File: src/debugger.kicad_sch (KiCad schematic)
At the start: 29 parts, among them J2 USB_C_Receptacle_USB2.0_14P, U7 RP2040, U8 W25Q128JVS, U9 NCP1117-1.5_SOT223, Y1 ABM8-272-T3

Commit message: revisão da RP2040
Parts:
- added J1: SM03B-SRSS-TB, Connector_JST:JST_SH_SM03B-SRSS-TB_1x03-1MP_P1.00mm_Horizontal, symbol Connector_Generic_MountingPin:Conn_01x03_MountingPin
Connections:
- net GND: now also J1.2 (Pin_2), J1.MP (MountPin)
- net QSPI_SCLK: no longer U7.52 (QSPI_SCLK)
- net QSPI_SD0: no longer U7.53 (QSPI_SD0)
- net QSPI_SD1: no longer U7.55 (QSPI_SD1)
- net QSPI_SD2: no longer U7.54 (QSPI_SD2)
- net QSPI_SD3: no longer U7.51 (QSPI_SD3)
- net QSPI_SS: no longer U7.56 (QSPI_SS)
- net XIN: no longer U7.20 (XIN)
- net XOUT: no longer U7.21 (XOUT)
- net SWCL renamed SWCLK
- net SWCLK: now also J1.1 (Pin_1)
- net UART1 RX renamed UART0 RX
- net UART1 TX renamed UART0 TX
- new net SWD: J1.3 (Pin_3)
- no-connect marks 26 -> 37
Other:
- note added: "CONECTOR"

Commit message: FEAT: adicionando footprints
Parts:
- J2: footprint (none) -> Connector_USB:USB_C_Receptacle_GCT_USB4105-xx-A_16P_TopMnt_Horizontal
- U7: footprint (none) -> componentes_personalizados:RP2040
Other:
- note added: "RP2040"
- moved on the sheet: C17, C18, C43, C44, C45, C47, C48, C49, C50, C51, C52, C59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

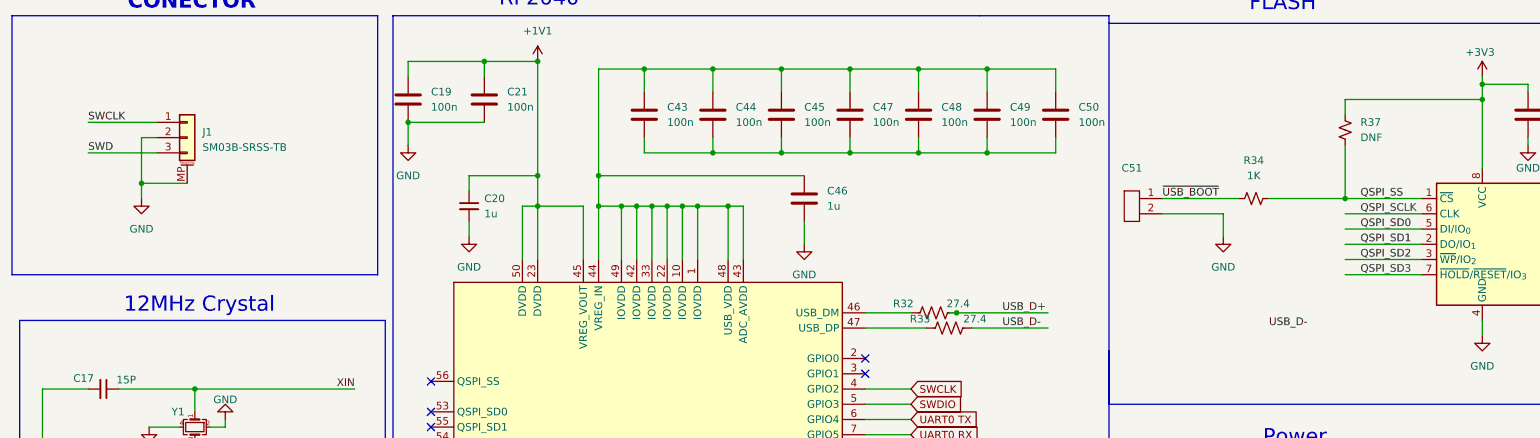
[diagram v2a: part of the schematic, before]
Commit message: adicionado footprints, falta microfone e display somente
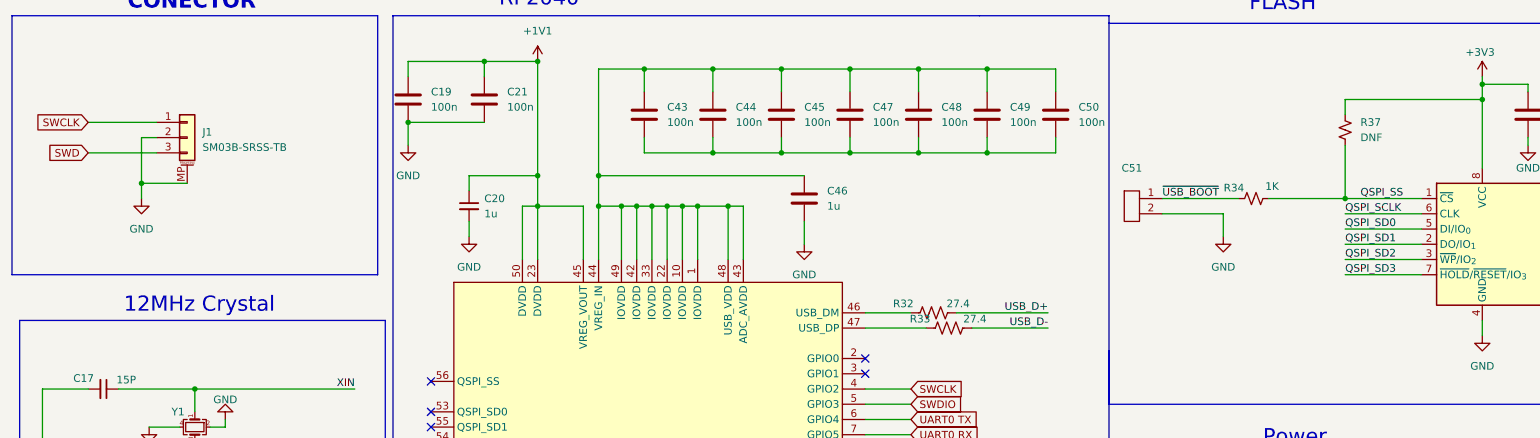
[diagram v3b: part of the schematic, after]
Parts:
- C51: footprint (none) -> Connector_PinHeader_1.00mm:PinHeader_1x02_P1.00mm_Horizontal
- R32, R33: footprint CR0402-FX-27R4GLF -> Resistor_SMD:R_0402_1005Metric
- R34, R37: footprint (none) -> Resistor_SMD:R_0402_1005Metric
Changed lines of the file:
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@@
 	)
 	(junction
-		(at 171.45 68.58)
-		(diameter 0)
-		(color 0 0 0 0)
-	)
-	(junction
 		(at 101.6 50.8)
 		(diameter 0)
@@
 	)
 	(no_connect
+		(at 156.21 76.2)
+	)
+	(no_connect
 		(at 156.21 137.16)
 	)
@@
 	)
 	(no_connect
-		(at 156.21 76.2)
-	)
-	(no_connect
 		(at 156.21 134.62)
 	)
@@
 	)
 	(no_connect
+		(at 156.21 114.3)
+	)
+	(no_connect
 		(at 156.21 78.74)
 	)
@@
 	)
 	(no_connect
-		(at 156.21 114.3)
-	)
-	(no_connect
 		(at 156.21 91.44)
 	)
@@
 	(wire
 		(pts
-			(xy 171.45 68.58) (xy 186.69 68.58)
-		)
-		(stroke
-			(width 0)
-			(type default)
-		)
-	)
-	(wire
-		(pts
 			(xy 133.35 50.8) (xy 135.89 50.8)
 		)
@@
 	(wire
 		(pts
-			(xy 236.22 62.23) (xy 248.92 62.23)
-		)
-		(stroke
-			(width 0)
-			(type default)
-		)
-	)
-	(wire
-		(pts
 			(xy 223.52 118.11) (xy 223.52 116.84)
 		)
@@
 	(wire
 		(pts
-			(xy 236.22 54.61) (xy 248.92 54.61)
-		)
-		(stroke
-			(width 0)
-			(type default)
-		)
-	)
-	(wire
-		(pts
 			(xy 259.08 30.48) (xy 266.7 30.48)
 		)
@@
 	(wire
 		(pts
-			(xy 236.22 59.69) (xy 248.92 59.69)
-		)
-		(stroke
-			(width 0)
-			(type default)
-		)
-	)
-	(wire
-		(pts
 			(xy 101.6 45.72) (xy 101.6 50.8)
 		)
@@
 	(wire
 		(pts
-			(xy 170.18 68.58) (xy 171.45 68.58)
-		)
-		(stroke
-			(width 0)
-			(type default)
-		)
-	)
-	(wire
-		(pts
 			(xy 212.09 125.73) (xy 228.6 125.73)
 		)
@@
 	(wire
 		(pts
+			(xy 236.22 62.23) (xy 248.92 62.23)
+		)
+		(stroke
+			(width 0)
+			(type default)
+		)
+	)
+	(wire
+		(pts
 			(xy 120.65 50.8) (xy 123.19 50.8)
 		)
@@
 		)
 	)
+	(wire
+		(pts
+			(xy 171.45 68.58) (xy 186.69 68.58)
+		)
+		(stroke
+			(width 0)
+			(type default)
+		)
+	)
 	(polyline
 		(pts
@@
 		)
 	)
+	(wire
+		(pts
+			(xy 236.22 59.69) (xy 248.92 59.69)
+		)
+		(stroke
+			(width 0)
+			(type default)
+		)
+	)
 	(polyline
 		(pts
@@
 	(wire
 		(pts
+			(xy 236.22 54.61) (xy 248.92 54.61)
+		)
+		(stroke
+			(width 0)
+			(type default)
+		)
+	)
+	(wire
+		(pts
 			(xy 101.6 50.8) (xy 99.06 50.8)
 		)
@@
 	)
 	(label "QSPI_SD3"
-		(at 238.76 62.23 0)
+		(at 236.22 62.23 0)
 		(effects
 			(font
@@
 		)
 	)
-	(label "USB_D-"
-		(at 223.52 71.12 0)
-		(effects
-			(font
-				(size 1.27 1.27)
-			)
-			(justify left bottom)
-		)
-	)
 	(label "XIN"
 		(at 71.12 81.28 180)
@@
 	)
 	(label "QSPI_SD1"
-		(at 238.76 57.15 0)
+		(at 236.22 57.15 0)
 		(effects
 			(font
@@
 	)
 	(label "QSPI_SD2"
-		(at 238.76 59.69 0)
+		(at 236.22 59.69 0)
 		(effects
 			(font
@@
 	)
 	(label "QSPI_SCLK"
-		(at 238.76 52.07 0)
+		(at 236.22 52.07 0)
 		(effects
 			(font
@@
 	)
 	(label "QSPI_SD0"
-		(at 238.76 54.61 0)
-		(effects
-			(font
-				(size 1.27 1.27)
-			)
-			(justify left bottom)
-		)
-	)
-	(label "SWD"
-		(at 26.67 41.91 0)
+		(at 236.22 54.61 0)
 		(effects
 			(font
@@
 	)
 	(label "USB_D-"
-		(at 179.07 71.12 0)
+		(at 186.69 71.12 180)
 		(effects
 			(font
 				(size 1.27 1.27)
 			)
-			(justify left bottom)
+			(justify right bottom)
 		)
 	)
 	(label "USB_D+"
-		(at 179.07 68.58 0)
+		(at 186.69 68.58 180)
 		(effects
 			(font
 				(size 1.27 1.27)
 			)
-			(justify left bottom)
-		)
-	)
-	(label "SWCLK"
-		(at 26.67 36.83 0)
-		(effects
-			(font
-				(size 1.27 1.27)
-			)
-			(justify left bottom)
+			(justify right bottom)
 		)
 	)
@@
 	(global_label "SWCLK"
 		(shape input)
+		(at 26.67 36.83 180)
+		(fields_autoplaced yes)
+		(effects
+			(font
+				(size 1.27 1.27)
+			)
+			(justify right)
+		)
+		(property "Intersheetrefs" "${INTERSHEET_REFS}"
+			(at 17.4558 36.83 0)
+			(effects
+				(font
+					(size 1.27 1.27)
+				)
+				(justify right)
+				(hide yes)
+			)
+		)
+	)
+	(global_label "SWCLK"
+		(shape input)
 		(at 163.83 81.28 0)
 		(fields_autoplaced yes)
@@
 		)
 	)
+	(global_label "SWD"
+		(shape input)
+		(at 26.67 41.91 180)
+		(fields_autoplaced yes)
+		(effects
+			(font
+				(size 1.27 1.27)
+			)
+			(justify right)
+		)
+		(property "Intersheetrefs" "${INTERSHEET_REFS}"
+			(at 19.7539 41.91 0)
+			(effects
+				(font
+					(size 1.27 1.27)
+				)
+				(justify right)
+				(hide yes)
+			)
+		)
+	)
 	(global_label "SWDIO"
 		(shape input)
@@
 			)
 		)
-		(property "Footprint" ""
+		(property "Footprint" "Connector_PinHeader_1.00mm:PinHeader_1x02_P1.00mm_Horizontal"
 			(at 198.12 45.72 0)
 			(effects
@@
 			)
 		)
-		(property "Footprint" "CR0402-FX-27R4GLF"
+		(property "Footprint" "Resistor_SMD:R_0402_1005Metric"
 			(at 170.434 70.104 90)
 			(effects
@@
 			)
 		)
-		(property "Footprint" ""
+		(property "Footprint" "Resistor_SMD:R_0402_1005Metric"
 			(at 236.22 38.1 0)
 			(effects
@@
 			)
 		)
-		(property "Footprint" "CR0402-FX-27R4GLF"
+		(property "Footprint" "Resistor_SMD:R_0402_1005Metric"
 			(at 167.894 67.564 90)
 			(effects
@@
 		(dnp no)
 		(property "Reference" "R34"
-			(at 220.98 43.18 90)
+			(at 217.678 47.752 90)
 			(effects
 				(font
@@
 		)
 		(property "Value" "1K"
-			(at 220.98 45.72 90)
+			(at 224.028 47.498 90)
 			(effects
 				(font
@@
 			)
 		)
-		(property "Footprint" ""
+		(property "Footprint" "Resistor_SMD:R_0402_1005Metric"
 			(at 220.98 49.53 0)
 			(effects

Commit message: pequenos ajustes nas tags
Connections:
- net SWD is gone; now on net SWDIO: J1.3 (Pin_3)
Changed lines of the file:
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@@
 		)
 	)
-	(global_label "SWD"
+	(global_label "SWDIO"
 		(shape input)
 		(at 26.67 41.91 180)
@@
 		)
 		(property "Intersheetrefs" "${INTERSHEET_REFS}"
-			(at 19.7539 41.91 0)
+			(at 17.8186 41.91 0)
 			(effects
 				(font

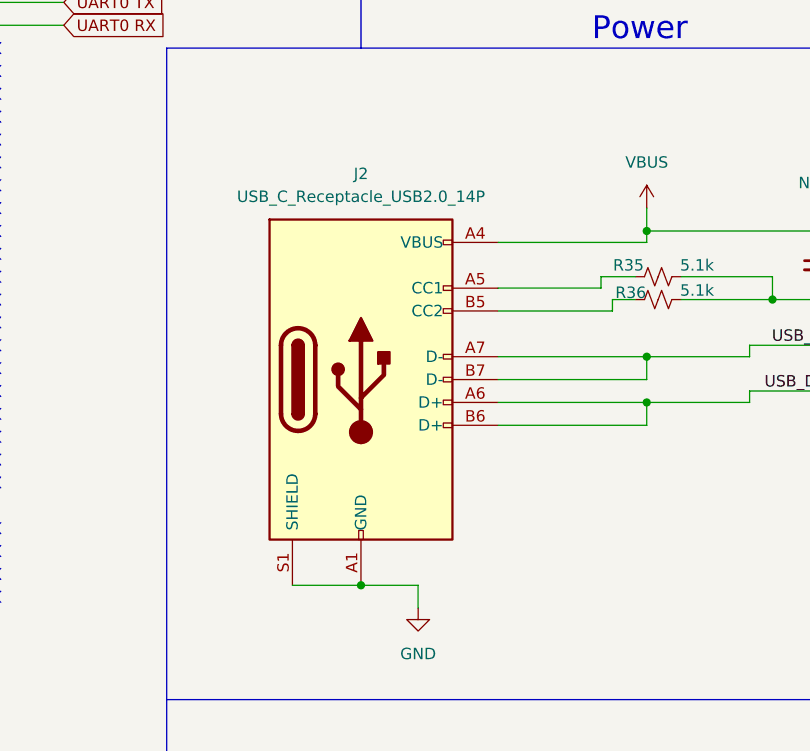
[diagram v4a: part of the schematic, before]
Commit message: Bugs na att da PCI resolvidos (falta só a tela OLED)
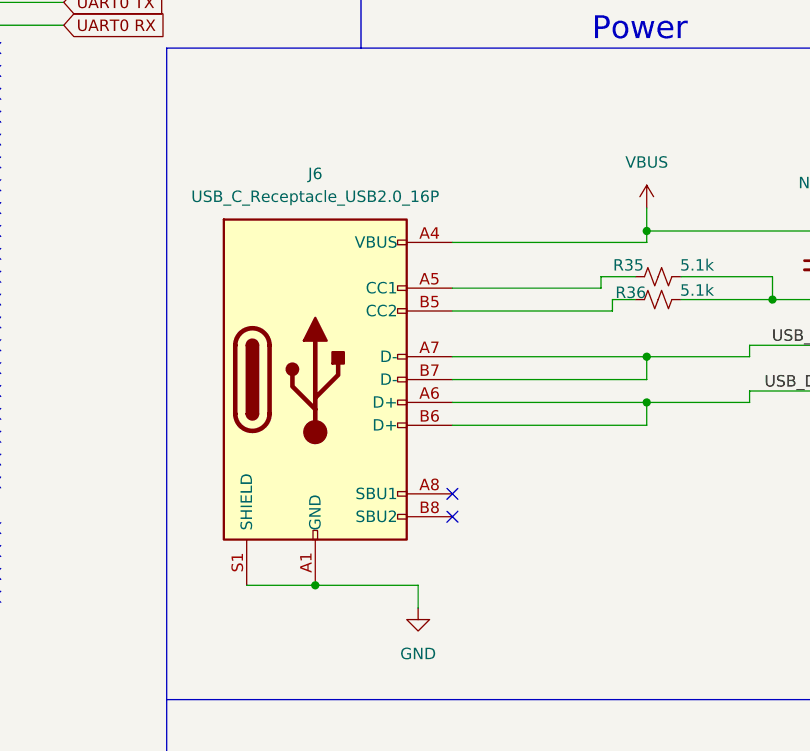
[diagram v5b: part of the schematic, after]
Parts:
- removed J2: USB_C_Receptacle_USB2.0_14P, Connector_USB:USB_C_Receptacle_GCT_USB4105-xx-A_16P_TopMnt_Horizontal, symbol Connector:USB_C_Receptacle_USB2.0_14P
- added J6: USB_C_Receptacle_USB2.0_16P, Connector_USB:USB_C_Receptacle_GCT_USB4105-xx-A_16P_TopMnt_Horizontal, symbol Connector:USB_C_Receptacle_USB2.0_16P
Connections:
- net GND: now also J6.A1 (GND), J6.A12 (GND), J6.B1 (GND), J6.B12 (GND), J6.S1 (SHIELD)
- net USB_D+: now also J6.A6 (D+), J6.B6 (D+)
- net USB_D-: now also J6.A7 (D-), J6.B7 (D-)
- net VBUS: now also J6.A4 (VBUS), J6.A9 (VBUS), J6.B4 (VBUS), J6.B9 (VBUS)
- net at R36.2: now also J6.B5 (CC2)
- net at R35.2: now also J6.A5 (CC1)
- no-connect marks 37 -> 39
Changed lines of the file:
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@@
 	)
 	(junction
+		(at 191.77 151.13)
+		(diameter 0)
+		(color 0 0 0 0)
+	)
+	(junction
 		(at 142.24 27.94)
 		(diameter 0)
@@
 	)
 	(junction
-		(at 196.85 151.13)
-		(diameter 0)
-		(color 0 0 0 0)
-	)
-	(junction
 		(at 101.6 45.72)
 		(diameter 0)
@@
 	)
 	(no_connect
+		(at 207.01 140.97)
+	)
+	(no_connect
 		(at 156.21 111.76)
 	)
@@
 	)
 	(no_connect
+		(at 207.01 143.51)
+	)
+	(no_connect
 		(at 156.21 147.32)
 	)
@@
 	(wire
 		(pts
-			(xy 196.85 151.13) (xy 203.2 151.13)
-		)
-		(stroke
-			(width 0)
-			(type default)
-		)
-	)
-	(wire
-		(pts
 			(xy 26.67 36.83) (xy 38.1 36.83)
 		)
@@
 	(wire
 		(pts
-			(xy 212.09 118.11) (xy 223.52 118.11)
+			(xy 207.01 118.11) (xy 223.52 118.11)
 		)
 		(stroke
@@
 	(wire
 		(pts
+			(xy 191.77 151.13) (xy 203.2 151.13)
+		)
+		(stroke
+			(width 0)
+			(type default)
+		)
+	)
+	(wire
+		(pts
 			(xy 228.6 113.03) (xy 228.6 111.76)
 		)
@@
 	(wire
 		(pts
-			(xy 212.09 125.73) (xy 228.6 125.73)
+			(xy 207.01 125.73) (xy 228.6 125.73)
 		)
 		(stroke
@@
 	(wire
 		(pts
-			(xy 212.09 120.65) (xy 224.79 120.65)
+			(xy 207.01 120.65) (xy 224.79 120.65)
 		)
 		(stroke
@@
 	(wire
 		(pts
-			(xy 212.09 113.03) (xy 228.6 113.03)
+			(xy 207.01 113.03) (xy 228.6 113.03)
 		)
 		(stroke
@@
 	(wire
 		(pts
-			(xy 212.09 130.81) (xy 228.6 130.81)
+			(xy 207.01 130.81) (xy 228.6 130.81)
 		)
 		(stroke
@@
 	(wire
 		(pts
-			(xy 189.23 151.13) (xy 196.85 151.13)
+			(xy 184.15 151.13) (xy 191.77 151.13)
 		)
 		(stroke
@@
 	(wire
 		(pts
-			(xy 228.6 128.27) (xy 212.09 128.27)
+			(xy 228.6 128.27) (xy 207.01 128.27)
 		)
 		(stroke
@@
 	(wire
 		(pts
-			(xy 228.6 133.35) (xy 212.09 133.35)
+			(xy 228.6 133.35) (xy 207.01 133.35)
 		)
 		(stroke
@@
 	)
 	(symbol
-		(lib_id "Connector:USB_C_Receptacle_USB2.0_14P")
-		(at 196.85 128.27 0)
-		(unit 1)
-		(exclude_from_sim no)
-		(in_bom yes)
-		(on_board yes)
-		(dnp no)
-		(fields_autoplaced yes)
-		(property "Reference" "J2"
-			(at 196.85 105.41 0)
-			(effects
-				(font
-					(size 1.27 1.27)
-				)
-			)
-		)
-		(property "Value" "USB_C_Receptacle_USB2.0_14P"
-			(at 196.85 107.95 0)
-			(effects
-				(font
-					(size 1.27 1.27)
-				)
-			)
-		)
-		(property "Footprint" "Connector_USB:USB_C_Receptacle_GCT_USB4105-xx-A_16P_TopMnt_Horizontal"
-			(at 200.66 128.27 0)
-			(effects
-				(font
-					(size 1.27 1.27)
-				)
-				(hide yes)
-			)
-		)
-		(property "Datasheet" "https://www.usb.org/sites/default/files/documents/usb_type-c.zip"
-			(at 200.66 128.27 0)
-			(effects
-				(font
-					(size 1.27 1.27)
-				)
-				(hide yes)
-			)
-		)
-		(property "Description" "USB 2.0-only 14P Type-C Receptacle connector"
-			(at 196.85 128.27 0)
-			(effects
-				(font
-					(size 1.27 1.27)
-				)
-				(hide yes)
-			)
-		)
-		(pin "A6"
-		)
-		(pin "S1"
-		)
-		(pin "A12"
-		)
-		(pin "A4"
-		)
-		(pin "A5"
-		)
-		(pin "B1"
-		)
-		(pin "B5"
-		)
-		(pin "A1"
-		)
-		(pin "B4"
-		)
-		(pin "A7"
-		)
-		(pin "B12"
-		)
-		(pin "B9"
-		)
-		(pin "A9"
-		)
-		(pin "B7"
-		)
-		(pin "B6"
-		)
-		(instances
-			(project "Circuitos Impressos"
-				(path "/49caf936-61f8-45e5-bebd-98db7502d055/3523909c-5026-4ff2-9976-775b6fedfefc"
-					(reference "J2")
-					(unit 1)
-				)
-			)
-		)
-	)
-	(symbol
 		(lib_id "power:GND")
 		(at 36.83 87.63 0)
@@
 					(unit 1)
 				)
+			)
+		)
+	)
+	(symbol
+		(lib_id "Connector:USB_C_Receptacle_USB2.0_16P")
+		(at 191.77 128.27 0)
+		(unit 1)
+		(exclude_from_sim no)
+		(in_bom yes)
+		(on_board yes)
+		(dnp no)
+		(fields_autoplaced yes)
+		(property "Reference" "J6"
+			(at 191.77 105.41 0)
+			(effects
+				(font
+					(size 1.27 1.27)
+				)
+			)
+		)
+		(property "Value" "USB_C_Receptacle_USB2.0_16P"
+			(at 191.77 107.95 0)
+			(effects
+				(font
+					(size 1.27 1.27)
+				)
+			)
+		)
+		(property "Footprint" "Connector_USB:USB_C_Receptacle_GCT_USB4105-xx-A_16P_TopMnt_Horizontal"
+			(at 195.58 128.27 0)
+			(effects
+				(font
+					(size 1.27 1.27)
+				)
+				(hide yes)
+			)
+		)
+		(property "Datasheet" "https://www.usb.org/sites/default/files/documents/usb_type-c.zip"
+			(at 195.58 128.27 0)
+			(effects
+				(font
+					(size 1.27 1.27)
+				)
+				(hide yes)
+			)
+		)
+		(property "Description" "USB 2.0-only 16P Type-C Receptacle connector"
+			(at 191.77 128.27 0)
+			(effects
+				(font
+					(size 1.27 1.27)
+				)
+				(hide yes)
+			)
+		)
+		(pin "A12"
+		)
+		(pin "S1"
+		)
+		(pin "A1"
+		)
+		(pin "A9"
+		)
+		(pin "B1"
+		)
+		(pin "A6"
+		)
+		(pin "A8"
+		)
+		(pin "B8"
+		)
+		(pin "B12"
+		)
+		(pin "B4"
+		)
+		(pin "B7"
+		)
+		(pin "B6"
+		)
+		(pin "A4"
+		)
+		(pin "A5"
+		)
+		(pin "A7"
+		)
+		(pin "B9"
+		)
+		(pin "B5"
+		)
+		(instances
+			(project ""
+				(path "/49caf936-61f8-45e5-bebd-98db7502d055/3523909c-5026-4ff2-9976-775b6fedfefc"
+					(reference "J6")
+					(unit 1)
+				)
